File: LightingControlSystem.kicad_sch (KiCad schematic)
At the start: 31 parts, among them J5 Physical Switch Terminal, J6 MOSFET Switch Module Terminal, U2 ESP32-DEVKIT-V1

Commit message: updated gerber files
re-add of resistor footprints -- for some reason it was removed
re-add of the new pull-down resistor R27 -- for some reason it was not
in the schematic but it exists in pcb
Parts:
- R10, R11, R12, R13, R14, R15, R16, R17, R18, R19, R20, R21, R22, R23, R24, R7, R8, R9: footprint (none) -> Resistor_THT:R_Axial_DIN0207_L6.3mm_D2.5mm_P7.62mm_Horizontal
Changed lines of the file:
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@@
 			)
 		)
-		(property "Footprint" ""
+		(property "Footprint" "Resistor_THT:R_Axial_DIN0207_L6.3mm_D2.5mm_P7.62mm_Horizontal"
 			(at 160.02 99.568 90)
 			(effects
@@
 			)
 		)
-		(property "Footprint" ""
+		(property "Footprint" "Resistor_THT:R_Axial_DIN0207_L6.3mm_D2.5mm_P7.62mm_Horizontal"
 			(at 191.77 77.978 90)
 			(effects
@@
 			)
 		)
-		(property "Footprint" ""
+		(property "Footprint" "Resistor_THT:R_Axial_DIN0207_L6.3mm_D2.5mm_P7.62mm_Horizontal"
 			(at 191.77 88.138 90)
 			(effects
@@
 			)
 		)
-		(property "Footprint" ""
+		(property "Footprint" "Resistor_THT:R_Axial_DIN0207_L6.3mm_D2.5mm_P7.62mm_Horizontal"
 			(at 99.06 102.108 90)
 			(effects
@@
 			)
 		)
-		(property "Footprint" ""
+		(property "Footprint" "Resistor_THT:R_Axial_DIN0207_L6.3mm_D2.5mm_P7.62mm_Horizontal"
 			(at 160.02 84.328 90)
 			(effects
@@
 			)
 		)
-		(property "Footprint" ""
+		(property "Footprint" "Resistor_THT:R_Axial_DIN0207_L6.3mm_D2.5mm_P7.62mm_Horizontal"
 			(at 92.202 68.58 90)
 			(effects
@@
 			)
 		)
-		(property "Footprint" ""
+		(property "Footprint" "Resistor_THT:R_Axial_DIN0207_L6.3mm_D2.5mm_P7.62mm_Horizontal"
 			(at 191.77 98.298 90)
 			(effects
@@
 			)
 		)
-		(property "Footprint" ""
+		(property "Footprint" "Resistor_THT:R_Axial_DIN0207_L6.3mm_D2.5mm_P7.62mm_Horizontal"
 			(at 160.02 91.948 90)
 			(effects
@@
 			)
 		)
-		(property "Footprint" ""
+		(property "Footprint" "Resistor_THT:R_Axial_DIN0207_L6.3mm_D2.5mm_P7.62mm_Horizontal"
 			(at 191.77 103.378 90)
 			(effects
@@
 			)
 		)
-		(property "Footprint" ""
+		(property "Footprint" "Resistor_THT:R_Axial_DIN0207_L6.3mm_D2.5mm_P7.62mm_Horizontal"
 			(at 191.77 108.458 90)
 			(effects
@@
 			)
 		)
-		(property "Footprint" ""
+		(property "Footprint" "Resistor_THT:R_Axial_DIN0207_L6.3mm_D2.5mm_P7.62mm_Horizontal"
 			(at 103.378 68.58 90)
 			(effects
@@
 			)
 		)
-		(property "Footprint" ""
+		(property "Footprint" "Resistor_THT:R_Axial_DIN0207_L6.3mm_D2.5mm_P7.62mm_Horizontal"
 			(at 191.77 83.058 90)
 			(effects
@@
 			)
 		)
-		(property "Footprint" ""
+		(property "Footprint" "Resistor_THT:R_Axial_DIN0207_L6.3mm_D2.5mm_P7.62mm_Horizontal"
 			(at 160.02 97.028 90)
 			(effects
@@
 			)
 		)
-		(property "Footprint" ""
+		(property "Footprint" "Resistor_THT:R_Axial_DIN0207_L6.3mm_D2.5mm_P7.62mm_Horizontal"
 			(at 191.77 93.218 90)
 			(effects
@@
 			)
 		)
-		(property "Footprint" ""
+		(property "Footprint" "Resistor_THT:R_Axial_DIN0207_L6.3mm_D2.5mm_P7.62mm_Horizontal"
 			(at 160.02 94.488 90)
 			(effects
@@
 			)
 		)
-		(property "Footprint" ""
+		(property "Footprint" "Resistor_THT:R_Axial_DIN0207_L6.3mm_D2.5mm_P7.62mm_Horizontal"
 			(at 160.02 81.788 90)
 			(effects
@@
 			)
 		)
-		(property "Footprint" ""
+		(property "Footprint" "Resistor_THT:R_Axial_DIN0207_L6.3mm_D2.5mm_P7.62mm_Horizontal"
 			(at 191.77 113.538 90)
 			(effects
@@
 			)
 		)
-		(property "Footprint" ""
+		(property "Footprint" "Resistor_THT:R_Axial_DIN0207_L6.3mm_D2.5mm_P7.62mm_Horizontal"
 			(at 99.06 99.568 90)
 			(effects

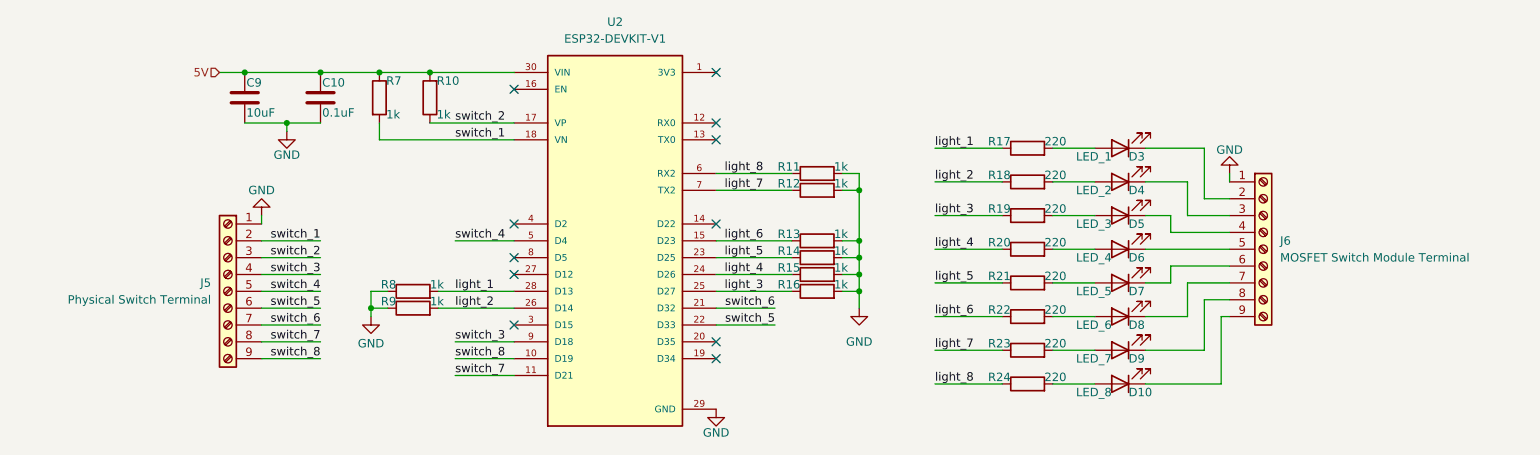
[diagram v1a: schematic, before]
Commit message: revision 2
modified pull-up/pull-down resistor values
modified switch1/switch2 input voltage from 5V to 3v3

added proper sheet detail (designer, cc license)
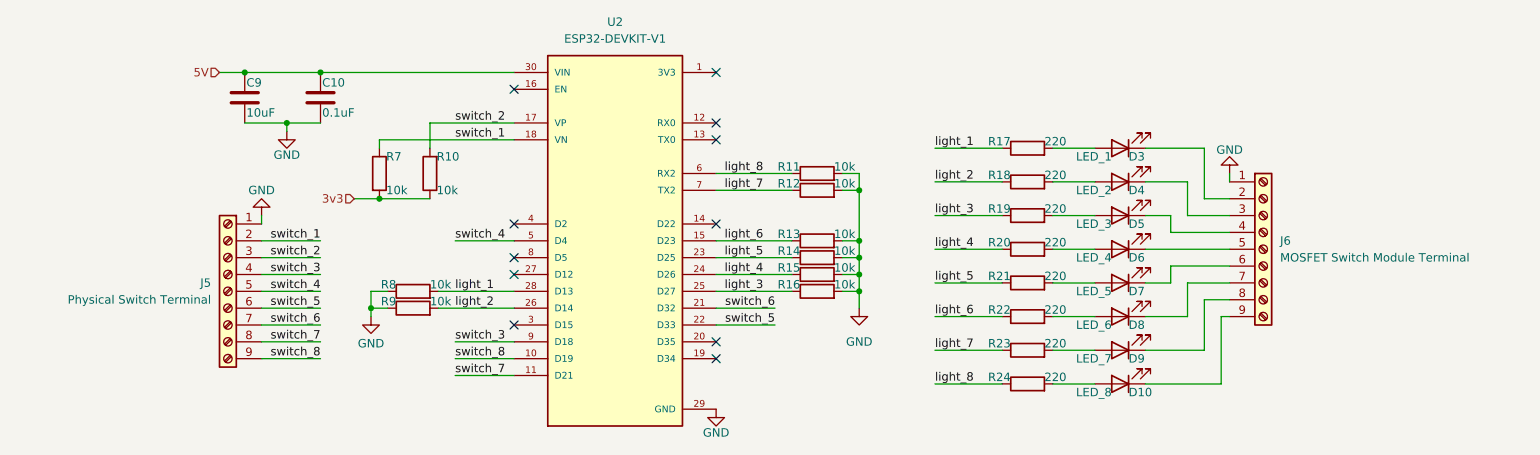
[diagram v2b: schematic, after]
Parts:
- R10, R11, R12, R13, R14, R15, R16, R7, R8, R9: value 1k -> 10k
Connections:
- net 5V: no longer R10.2, R7.1
- net switch_1: now also R7.1; no longer R7.2
- net switch_2: now also R10.2; no longer R10.1
- new net 3v3: R10.1, R7.2
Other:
- moved on the sheet: R10, R7
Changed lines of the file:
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@@
 		(title "Lighting Control System")
 		(date "2025-10-31")
-		(rev "0")
+		(rev "2")
+		(comment 1 "Designed by: Sidney Manzano")
+		(comment 2 "Released under the Creative Commons")
+		(comment 3 "Attribution Share-Alike 4.0 License")
+		(comment 4 "https://creativecommons.org/licenses/by-sa/4.0")
 	)
 	(junction
@@
 	)
 	(junction
-		(at 101.6 64.77)
-		(diameter 0)
-		(color 0 0 0 0)
-	)
-	(junction
 		(at 166.37 90.17)
 		(diameter 0)
@@
 	)
 	(junction
-		(at 93.98 64.77)
-		(diameter 0)
-		(color 0 0 0 0)
-	)
-	(junction
 		(at 166.37 82.55)
 		(diameter 0)
@@
 		(color 0 0 0 0)
 	)
+	(junction
+		(at 93.98 83.82)
+		(diameter 0)
+		(color 0 0 0 0)
+	)
 	(no_connect
 		(at 114.3 92.71)
@@
 	(wire
 		(pts
-			(xy 93.98 64.77) (xy 101.6 64.77)
-		)
-		(stroke
-			(width 0)
-			(type default)
-		)
-	)
-	(wire
-		(pts
 			(xy 218.44 99.06) (xy 222.25 99.06)
 		)
@@
 	(wire
 		(pts
-			(xy 101.6 72.39) (xy 114.3 72.39)
-		)
-		(stroke
-			(width 0)
-			(type default)
-		)
-	)
-	(wire
-		(pts
 			(xy 177.8 111.76) (xy 187.96 111.76)
 		)
@@
 	(wire
 		(pts
+			(xy 93.98 83.82) (xy 101.6 83.82)
+		)
+		(stroke
+			(width 0)
+			(type default)
+		)
+	)
+	(wire
+		(pts
 			(xy 93.98 74.93) (xy 114.3 74.93)
 		)
@@
 	(wire
 		(pts
+			(xy 101.6 72.39) (xy 114.3 72.39)
+		)
+		(stroke
+			(width 0)
+			(type default)
+		)
+	)
+	(wire
+		(pts
 			(xy 195.58 91.44) (xy 201.93 91.44)
 		)
@@
 	(wire
 		(pts
-			(xy 218.44 106.68) (xy 218.44 99.06)
+			(xy 90.17 83.82) (xy 93.98 83.82)
 		)
 		(stroke
@@
 	(wire
 		(pts
-			(xy 105.41 90.17) (xy 114.3 90.17)
+			(xy 218.44 106.68) (xy 218.44 99.06)
 		)
 		(stroke
@@
 	(wire
 		(pts
-			(xy 215.9 96.52) (xy 222.25 96.52)
+			(xy 105.41 90.17) (xy 114.3 90.17)
 		)
 		(stroke
@@
 	(wire
 		(pts
-			(xy 85.09 64.77) (xy 93.98 64.77)
+			(xy 215.9 96.52) (xy 222.25 96.52)
 		)
 		(stroke
@@
 	(wire
 		(pts
+			(xy 93.98 76.2) (xy 93.98 74.93)
+		)
+		(stroke
+			(width 0)
+			(type default)
+		)
+	)
+	(wire
+		(pts
 			(xy 92.71 100.33) (xy 92.71 101.6)
 		)
@@
 	(wire
 		(pts
-			(xy 93.98 72.39) (xy 93.98 74.93)
+			(xy 218.44 83.82) (xy 222.25 83.82)
 		)
 		(stroke
@@
 	(wire
 		(pts
-			(xy 218.44 83.82) (xy 222.25 83.82)
+			(xy 166.37 82.55) (xy 166.37 90.17)
 		)
 		(stroke
@@
 	(wire
 		(pts
-			(xy 166.37 82.55) (xy 166.37 90.17)
+			(xy 80.01 73.66) (xy 80.01 72.39)
 		)
 		(stroke
@@
 	(wire
 		(pts
-			(xy 80.01 73.66) (xy 80.01 72.39)
+			(xy 76.2 86.36) (xy 76.2 87.63)
 		)
 		(stroke
@@
 	(wire
 		(pts
-			(xy 76.2 86.36) (xy 76.2 87.63)
+			(xy 101.6 72.39) (xy 101.6 76.2)
 		)
 		(stroke
@@
 	(wire
 		(pts
-			(xy 101.6 64.77) (xy 114.3 64.77)
+			(xy 85.09 64.77) (xy 114.3 64.77)
 		)
 		(stroke
@@
 		)
 	)
+	(hierarchical_label "3v3"
+		(shape input)
+		(at 90.17 83.82 180)
+		(effects
+			(font
+				(size 1.27 1.27)
+			)
+			(justify right)
+		)
+	)
 	(hierarchical_label "5V"
 		(shape input)
@@
 			)
 		)
-		(property "Value" "1k"
+		(property "Value" "10k"
 			(at 162.56 96.774 90)
 			(effects
@@
 			)
 		)
-		(property "Value" "1k"
+		(property "Value" "10k"
 			(at 101.6 99.314 90)
 			(effects
@@
 			)
 		)
-		(property "Value" "1k"
+		(property "Value" "10k"
 			(at 162.56 81.534 90)
 			(effects
@@
 	(symbol
 		(lib_id "Device:R")
-		(at 93.98 68.58 0)
+		(at 93.98 80.01 0)
 		(unit 1)
 		(exclude_from_sim no)
@@
 		(dnp no)
 		(property "Reference" "R7"
-			(at 94.996 66.04 0)
+			(at 94.996 77.47 0)
 			(effects
 				(font
@@
 			)
 		)
-		(property "Value" "1k"
-			(at 94.996 71.12 0)
+		(property "Value" "10k"
+			(at 94.996 82.55 0)
 			(effects
 				(font
@@
 		)
 		(property "Footprint" "Resistor_THT:R_Axial_DIN0207_L6.3mm_D2.5mm_P7.62mm_Horizontal"
-			(at 92.202 68.58 90)
+			(at 92.202 80.01 90)
 			(effects
 				(font
@@
 		)
 		(property "Datasheet" "~"
-			(at 93.98 68.58 0)
+			(at 93.98 80.01 0)
 			(effects
 				(font
@@
 		)
 		(property "Description" "Resistor"
-			(at 93.98 68.58 0)
+			(at 93.98 80.01 0)
 			(effects
 				(font
@@
 			)
 		)
-		(property "Value" "1k"
+		(property "Value" "10k"
 			(at 162.56 89.154 90)
 			(effects
@@
 	(symbol
 		(lib_id "Device:R")
-		(at 101.6 68.58 180)
+		(at 101.6 80.01 180)
 		(unit 1)
 		(exclude_from_sim no)
@@
 		(dnp no)
 		(property "Reference" "R10"
-			(at 102.616 66.04 0)
+			(at 102.616 77.47 0)
 			(effects
 				(font
@@
 			)
 		)
-		(property "Value" "1k"
-			(at 102.616 71.12 0)
+		(property "Value" "10k"
+			(at 102.616 82.55 0)
 			(effects
 				(font
@@
 		)
 		(property "Footprint" "Resistor_THT:R_Axial_DIN0207_L6.3mm_D2.5mm_P7.62mm_Horizontal"
-			(at 103.378 68.58 90)
+			(at 103.378 80.01 90)
 			(effects
 				(font
@@
 		)
 		(property "Datasheet" "~"
-			(at 101.6 68.58 0)
+			(at 101.6 80.01 0)
 			(effects
 				(font
@@
 		)
 		(property "Description" "Resistor"
-			(at 101.6 68.58 0)
+			(at 101.6 80.01 0)
 			(effects
 				(font
@@
 			)
 		)
-		(property "Value" "1k"
+		(property "Value" "10k"
 			(at 162.56 94.234 90)
 			(effects
@@
 			)
 		)
-		(property "Value" "1k"
+		(property "Value" "10k"
 			(at 162.56 91.694 90)
 			(effects
@@
 			)
 		)
-		(property "Value" "1k"
+		(property "Value" "10k"
 			(at 162.56 78.994 90)
 			(effects
@@
 			)
 		)
-		(property "Value" "1k"
+		(property "Value" "10k"
 			(at 101.6 96.774 90)
 			(effects
